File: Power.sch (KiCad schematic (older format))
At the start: 0 parts

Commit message: Wire up Power Schematic
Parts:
- added C? (x2): C, ~, symbol C
- added F? (x4): FUSE, ~, symbol FUSE
- added L? (x2): INDUCTOR, ~, symbol INDUCTOR
- added P?: CONN_12X2, symbol CONN_12X2
- added R?: R, ~, symbol R
- added SW?: SWITCH_INV, ~, symbol SWITCH_INV
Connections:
- net labels added: +12P, +12V, +3.3V, +5V, -12P, -12V, GND
- wire segments 0 -> 37

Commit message: Upgrade Current/Fan Output Schem Use PWM
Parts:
- removed F? (x4): FUSE, ~, symbol FUSE
- added TH? (x4): THERMISTOR, ~, symbol THERMISTOR
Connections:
- net labels added: +12C
- wire segments 37 -> 44
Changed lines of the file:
@@
 $Descr A4 11693 8268
 encoding utf-8
-Sheet 4 9
+Sheet 3 9
 Title ""
-Date "5 feb 2014"
+Date "9 feb 2014"
 Rev ""
 Comp ""
@@
 $EndComp
 $Comp
-L FUSE F?
-U 1 1 52F247FD
-P 3100 1600
-F 0 "F?" H 3200 1650 40  0000 C CNN
-F 1 "FUSE" H 3000 1550 40  0000 C CNN
-F 2 "~" H 3100 1600 60  0000 C CNN
-F 3 "~" H 3100 1600 60  0000 C CNN
-	1    3100 1600
-	1    0    0    -1
-$EndComp
-$Comp
-L FUSE F?
-U 1 1 52F24814
-P 3700 1800
-F 0 "F?" H 3800 1850 40  0000 C CNN
-F 1 "FUSE" H 3600 1750 40  0000 C CNN
-F 2 "~" H 3700 1800 60  0000 C CNN
-F 3 "~" H 3700 1800 60  0000 C CNN
-	1    3700 1800
-	1    0    0    -1
-$EndComp
-$Comp
-L FUSE F?
-U 1 1 52F2481A
-P 4350 2000
-F 0 "F?" H 4450 2050 40  0000 C CNN
-F 1 "FUSE" H 4250 1950 40  0000 C CNN
-F 2 "~" H 4350 2000 60  0000 C CNN
-F 3 "~" H 4350 2000 60  0000 C CNN
-	1    4350 2000
-	1    0    0    -1
-$EndComp
-$Comp
-L FUSE F?
-U 1 1 52F24820
-P 4750 2200
-F 0 "F?" H 4850 2250 40  0000 C CNN
-F 1 "FUSE" H 4650 2150 40  0000 C CNN
-F 2 "~" H 4750 2200 60  0000 C CNN
-F 3 "~" H 4750 2200 60  0000 C CNN
-	1    4750 2200
-	1    0    0    -1
-$EndComp
-$Comp
 L SWITCH_INV SW?
 U 1 1 52F24828
@@
 $EndComp
 Wire Wire Line
-	900  1700 1850 1700
+	900  1700 1500 1700
+Wire Wire Line
+	1500 1700 1850 1700
 Wire Wire Line
 	900  1700 900  1850
 Wire Wire Line
-	2650 1600 2850 1600
-Wire Wire Line
-	3300 1600 3800 1600
+	3400 1600 3800 1600
 Wire Wire Line
 	3800 1600 3800 1000
@@
 	2850 1700 2850 1800
 Wire Wire Line
-	2650 1800 3450 1800
+	2650 1800 2850 1800
+Wire Wire Line
+	2850 1800 3450 1800
 Connection ~ 2850 1800
 Wire Wire Line
@@
 	4200 1800 4200 1000
 Wire Wire Line
-	2650 2000 4100 2000
+	2650 2000 2750 2000
+Wire Wire Line
+	2750 2000 4100 2000
 Wire Wire Line
 	2650 2200 4500 2200
@@
 $EndComp
 Wire Wire Line
-	7800 2400 9000 2400
-Wire Wire Line
-	8450 1750 8450 2000
-Wire Wire Line
-	7800 1350 9050 1350
+	7800 2400 8450 2400
+Wire Wire Line
+	8450 2400 9000 2400
+Wire Wire Line
+	8450 1750 8450 1850
+Wire Wire Line
+	8450 1850 8450 2000
+Wire Wire Line
+	7800 1350 8450 1350
+Wire Wire Line
+	8450 1350 9050 1350
 Wire Wire Line
 	8000 1900 8000 1850
@@
 Wire Wire Line
 	6950 1350 7200 1350
+$Comp
+L THERMISTOR TH?
+U 1 1 52F79925
+P 3150 1600
+F 0 "TH?" V 3250 1650 50  0000 C CNN
+F 1 "THERMISTOR" V 3050 1600 50  0000 C CNN
+F 2 "~" H 3150 1600 60  0000 C CNN
+F 3 "~" H 3150 1600 60  0000 C CNN
+	1    3150 1600
+	0    -1   -1   0
+$EndComp
+$Comp
+L THERMISTOR TH?
+U 1 1 52F79932
+P 3700 1800
+F 0 "TH?" V 3800 1850 50  0000 C CNN
+F 1 "THERMISTOR" V 3600 1800 50  0000 C CNN
+F 2 "~" H 3700 1800 60  0000 C CNN
+F 3 "~" H 3700 1800 60  0000 C CNN
+	1    3700 1800
+	0    -1   -1   0
+$EndComp
+$Comp
+L THERMISTOR TH?
+U 1 1 52F79938
+P 4350 2000
+F 0 "TH?" V 4450 2050 50  0000 C CNN
+F 1 "THERMISTOR" V 4250 2000 50  0000 C CNN
+F 2 "~" H 4350 2000 60  0000 C CNN
+F 3 "~" H 4350 2000 60  0000 C CNN
+	1    4350 2000
+	0    -1   -1   0
+$EndComp
+$Comp
+L THERMISTOR TH?
+U 1 1 52F7993E
+P 4750 2200
+F 0 "TH?" V 4850 2250 50  0000 C CNN
+F 1 "THERMISTOR" V 4650 2200 50  0000 C CNN
+F 2 "~" H 4750 2200 60  0000 C CNN
+F 3 "~" H 4750 2200 60  0000 C CNN
+	1    4750 2200
+	0    -1   -1   0
+$EndComp
+Wire Wire Line
+	2900 1600 2650 1600
+Wire Wire Line
+	2750 2000 2750 1200
+Connection ~ 2750 2000
+$Comp
+L +12C #PWR?
+U 1 1 52F7999C
+P 2750 1200
+F 0 "#PWR?" H 2750 1170 30  0001 C CNN
+F 1 "+12C" H 2750 1310 40  0000 C CNN
+F 2 "" H 2750 1200 60  0000 C CNN
+F 3 "" H 2750 1200 60  0000 C CNN
+	1    2750 1200
+	1    0    0    -1
+$EndComp
 $EndSCHEMATC

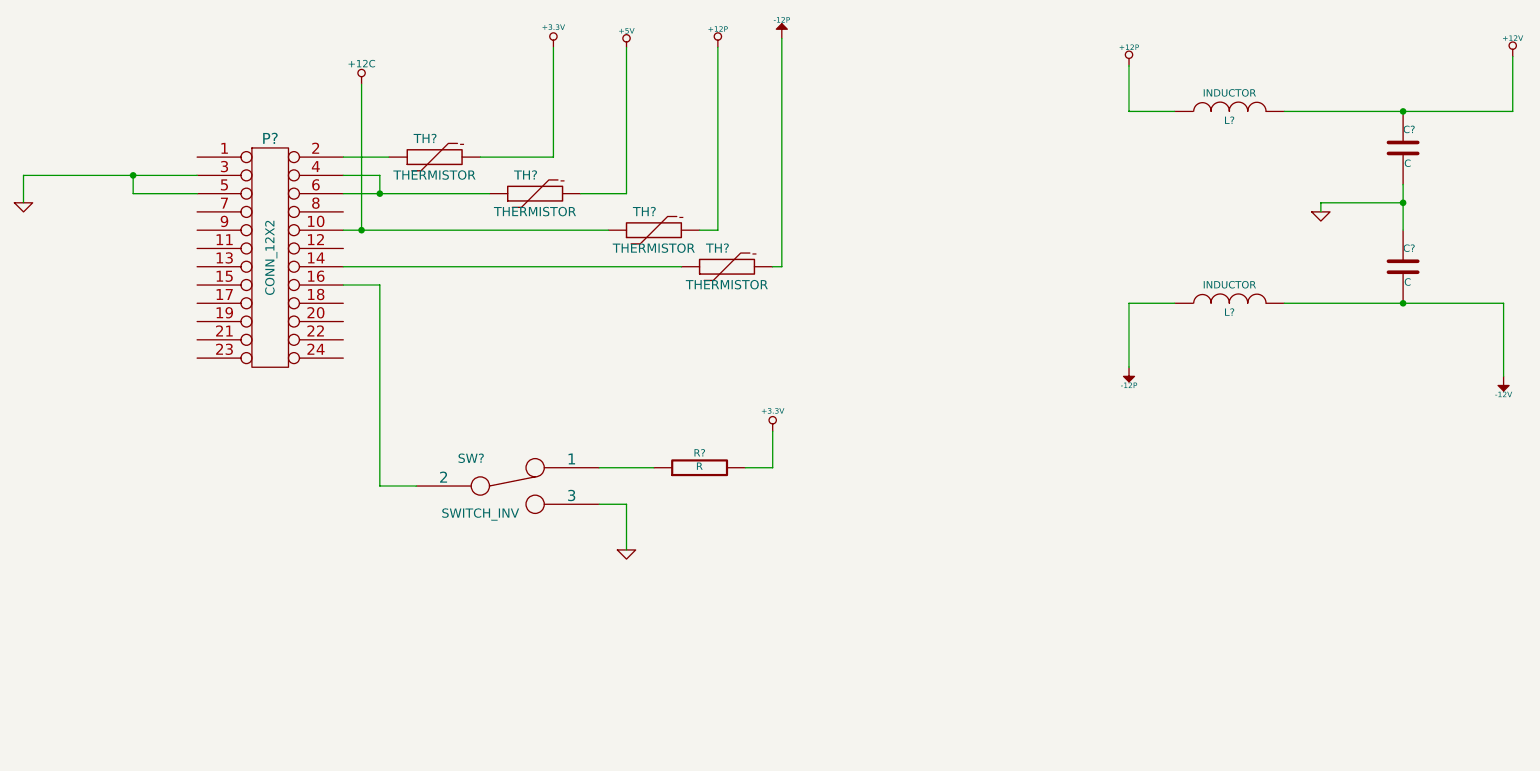
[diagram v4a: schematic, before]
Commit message: Added Arduino Connect Pin Layout
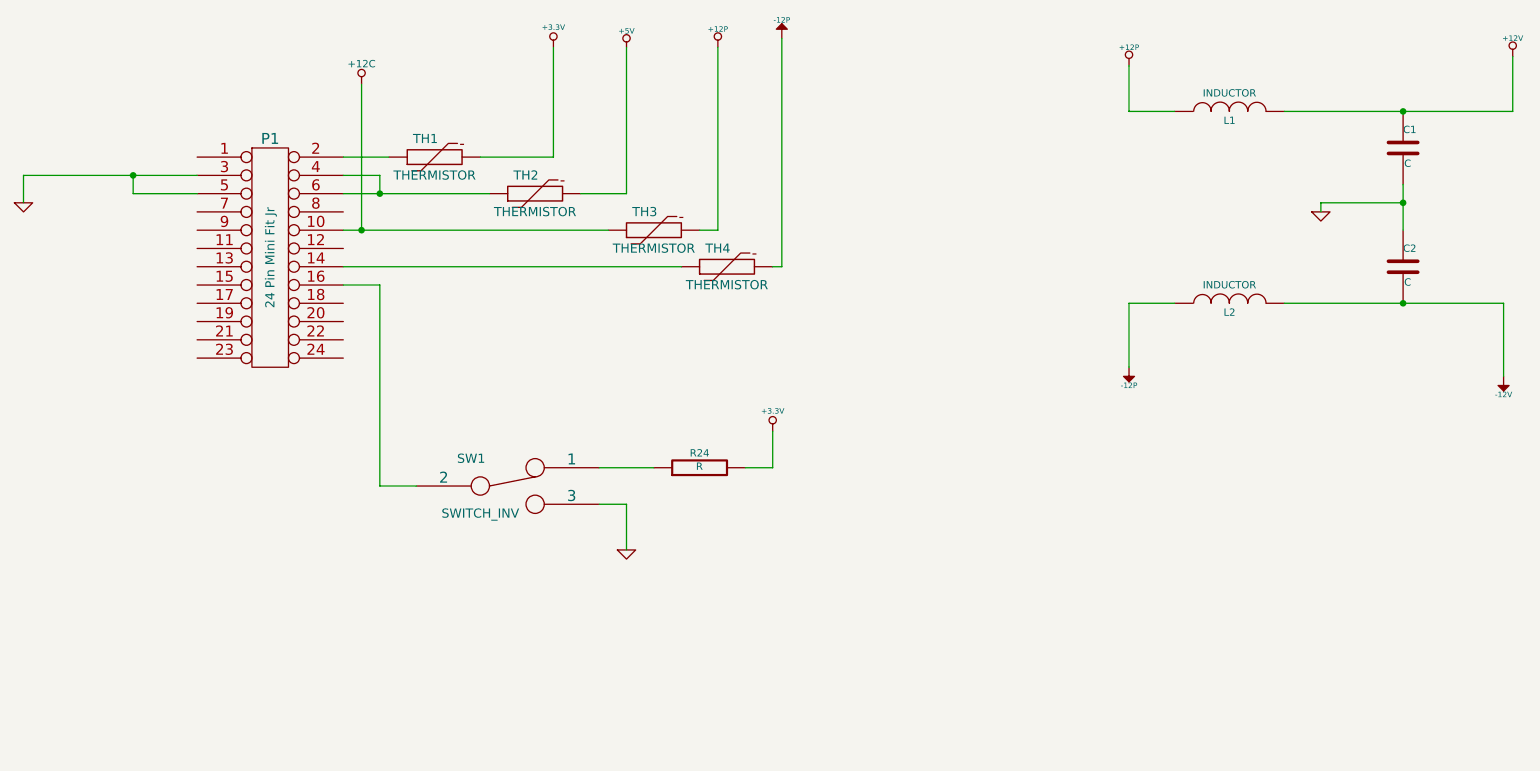
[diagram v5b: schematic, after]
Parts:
- P1: renamed from P?; value CONN_12X2 -> 24 Pin Mini Fit Jr; MFG Name (none) -> Molex; MFG Part Number (none) -> 39-30-1240
- gave numbers to parts that had none: 10
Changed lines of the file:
@@
 $EndDescr
 $Comp
-L CONN_12X2 P?
+L CONN_12X2 P1
 U 1 1 52F24792
 P 2250 2150
-F 0 "P?" H 2250 2800 60  0000 C CNN
-F 1 "CONN_12X2" V 2250 2150 50  0000 C CNN
+F 0 "P1" H 2250 2800 60  0000 C CNN
+F 1 "24 Pin Mini Fit Jr" V 2250 2150 50  0000 C CNN
 F 2 "" H 2250 2150 60  0000 C CNN
 F 3 "" H 2250 2150 60  0000 C CNN
+F 4 "Molex" H 2250 2150 60  0001 C CNN "MFG Name"
+F 5 "39-30-1240" H 2250 2150 60  0001 C CNN "MFG Part Number"
 	1    2250 2150
 	1    0    0    -1
 $EndComp
 $Comp
-L GND #PWR?
+L GND #PWR3
 U 1 1 52F247A1
 P 900 1850
-F 0 "#PWR?" H 900 1850 30  0001 C CNN
+F 0 "#PWR3" H 900 1850 30  0001 C CNN
 F 1 "GND" H 900 1780 30  0001 C CNN
 F 2 "" H 900 1850 60  0000 C CNN
@@
 $EndComp
 $Comp
-L +3.3V #PWR?
+L +3.3V #PWR5
 U 1 1 52F247B1
 P 3800 1000
-F 0 "#PWR?" H 3800 960 30  0001 C CNN
+F 0 "#PWR5" H 3800 960 30  0001 C CNN
 F 1 "+3.3V" H 3800 1110 30  0000 C CNN
 F 2 "" H 3800 1000 60  0000 C CNN
@@
 $EndComp
 $Comp
-L +5V #PWR?
+L +5V #PWR6
 U 1 1 52F247C3
 P 4200 1000
-F 0 "#PWR?" H 4200 1090 20  0001 C CNN
+F 0 "#PWR6" H 4200 1090 20  0001 C CNN
 F 1 "+5V" H 4200 1090 30  0000 C CNN
 F 2 "" H 4200 1000 60  0000 C CNN
@@
 $EndComp
 $Comp
-L SWITCH_INV SW?
+L SWITCH_INV SW1
 U 1 1 52F24828
 P 3550 3400
-F 0 "SW?" H 3350 3550 50  0000 C CNN
+F 0 "SW1" H 3350 3550 50  0000 C CNN
 F 1 "SWITCH_INV" H 3400 3250 50  0000 C CNN
 F 2 "~" H 3550 3400 60  0000 C CNN
@@
 $EndComp
 $Comp
-L +12P #PWR?
+L +12P #PWR8
 U 1 1 52F248B4
 P 4700 1000
-F 0 "#PWR?" H 4700 970 30  0001 C CNN
+F 0 "#PWR8" H 4700 970 30  0001 C CNN
 F 1 "+12P" H 4700 1100 30  0000 C CNN
 F 2 "" H 4700 1000 60  0000 C CNN
@@
 $EndComp
 $Comp
-L -12P #PWR?
+L -12P #PWR10
 U 1 1 52F24F25
 P 5050 950
-F 0 "#PWR?" H 5050 1080 20  0001 C CNN
+F 0 "#PWR10" H 5050 1080 20  0001 C CNN
 F 1 "-12P" H 5050 1050 30  0000 C CNN
 F 2 "" H 5050 950 60  0000 C CNN
@@
 $EndComp
 $Comp
-L GND #PWR?
+L GND #PWR7
 U 1 1 52F24F77
 P 4200 3750
-F 0 "#PWR?" H 4200 3750 30  0001 C CNN
+F 0 "#PWR7" H 4200 3750 30  0001 C CNN
 F 1 "GND" H 4200 3680 30  0001 C CNN
 F 2 "" H 4200 3750 60  0000 C CNN
@@
 $EndComp
 $Comp
-L R R?
+L R R24
 U 1 1 52F24FB1
 P 4600 3300
-F 0 "R?" V 4680 3300 40  0000 C CNN
+F 0 "R24" V 4680 3300 40  0000 C CNN
 F 1 "R" V 4607 3301 40  0000 C CNN
 F 2 "~" V 4530 3300 30  0000 C CNN
@@
 $EndComp
 $Comp
-L +3.3V #PWR?
+L +3.3V #PWR9
 U 1 1 52F24FD9
 P 5000 3100
-F 0 "#PWR?" H 5000 3060 30  0001 C CNN
+F 0 "#PWR9" H 5000 3060 30  0001 C CNN
 F 1 "+3.3V" H 5000 3210 30  0000 C CNN
 F 2 "" H 5000 3100 60  0000 C CNN
@@
 $EndComp
 Wire Wire Line
-	900  1700 1500 1700
-Wire Wire Line
-	1500 1700 1850 1700
+	900  1700 1850 1700
 Wire Wire Line
 	900  1700 900  1850
@@
 	2850 1700 2850 1800
 Wire Wire Line
-	2650 1800 2850 1800
-Wire Wire Line
-	2850 1800 3450 1800
+	2650 1800 3450 1800
 Connection ~ 2850 1800
 Wire Wire Line
@@
 	4200 1800 4200 1000
 Wire Wire Line
-	2650 2000 2750 2000
-Wire Wire Line
-	2750 2000 4100 2000
+	2650 2000 4100 2000
 Wire Wire Line
 	2650 2200 4500 2200
@@
 	5000 3100 5000 3300
 $Comp
-L -12P #PWR?
+L -12P #PWR12
 U 1 1 52F251E3
 P 6950 2750
-F 0 "#PWR?" H 6950 2880 20  0001 C CNN
+F 0 "#PWR12" H 6950 2880 20  0001 C CNN
 F 1 "-12P" H 6950 2850 30  0000 C CNN
 F 2 "" H 6950 2750 60  0000 C CNN
@@
 $EndComp
 $Comp
-L +12P #PWR?
+L +12P #PWR11
 U 1 1 52F251E9
 P 6950 1100
-F 0 "#PWR?" H 6950 1070 30  0001 C CNN
+F 0 "#PWR11" H 6950 1070 30  0001 C CNN
 F 1 "+12P" H 6950 1200 30  0000 C CNN
 F 2 "" H 6950 1100 60  0000 C CNN
@@
 $EndComp
 $Comp
-L GND #PWR?
+L GND #PWR13
 U 1 1 52F251EF
 P 8000 1900
-F 0 "#PWR?" H 8000 1900 30  0001 C CNN
+F 0 "#PWR13" H 8000 1900 30  0001 C CNN
 F 1 "GND" H 8000 1830 30  0001 C CNN
 F 2 "" H 8000 1900 60  0000 C CNN
@@
 $EndComp
 $Comp
-L INDUCTOR L?
+L INDUCTOR L1
 U 1 1 52F2522D
 P 7500 1350
-F 0 "L?" V 7450 1350 40  0000 C CNN
+F 0 "L1" V 7450 1350 40  0000 C CNN
 F 1 "INDUCTOR" V 7600 1350 40  0000 C CNN
 F 2 "~" H 7500 1350 60  0000 C CNN
@@
 $EndComp
 $Comp
-L INDUCTOR L?
+L INDUCTOR L2
 U 1 1 52F2523A
 P 7500 2400
-F 0 "L?" V 7450 2400 40  0000 C CNN
+F 0 "L2" V 7450 2400 40  0000 C CNN
 F 1 "INDUCTOR" V 7600 2400 40  0000 C CNN
 F 2 "~" H 7500 2400 60  0000 C CNN
@@
 $EndComp
 $Comp
-L C C?
+L C C1
 U 1 1 52F25242
 P 8450 1550
-F 0 "C?" H 8450 1650 40  0000 L CNN
+F 0 "C1" H 8450 1650 40  0000 L CNN
 F 1 "C" H 8456 1465 40  0000 L CNN
 F 2 "~" H 8488 1400 30  0000 C CNN
@@
 $EndComp
 $Comp
-L C C?
+L C C2
 U 1 1 52F2524F
 P 8450 2200
-F 0 "C?" H 8450 2300 40  0000 L CNN
+F 0 "C2" H 8450 2300 40  0000 L CNN
 F 1 "C" H 8456 2115 40  0000 L CNN
 F 2 "~" H 8488 2050 30  0000 C CNN
@@
 $EndComp
 Wire Wire Line
-	7800 2400 8450 2400
-Wire Wire Line
-	8450 2400 9000 2400
-Wire Wire Line
-	8450 1750 8450 1850
-Wire Wire Line
-	8450 1850 8450 2000
-Wire Wire Line
-	7800 1350 8450 1350
-Wire Wire Line
-	8450 1350 9050 1350
+	7800 2400 9000 2400
+Wire Wire Line
+	8450 1750 8450 2000
+Wire Wire Line
+	7800 1350 9050 1350
 Wire Wire Line
 	8000 1900 8000 1850
@@
 Connection ~ 8450 1850
 $Comp
-L +12V #PWR?
+L +12V #PWR15
 U 1 1 52F2533A
 P 9050 1050
-F 0 "#PWR?" H 9050 1000 20  0001 C CNN
+F 0 "#PWR15" H 9050 1000 20  0001 C CNN
 F 1 "+12V" H 9050 1150 30  0000 C CNN
 F 2 "" H 9050 1050 60  0000 C CNN
@@
 $EndComp
 $Comp
-L -12V #PWR?
+L -12V #PWR14
 U 1 1 52F25349
 P 9000 2800
-F 0 "#PWR?" H 9000 2930 20  0001 C CNN
+F 0 "#PWR14" H 9000 2930 20  0001 C CNN
 F 1 "-12V" H 9000 2900 30  0000 C CNN
 F 2 "" H 9000 2800 60  0000 C CNN
@@
 	6950 1350 7200 1350
 $Comp
-L THERMISTOR TH?
+L THERMISTOR TH1
 U 1 1 52F79925
 P 3150 1600
-F 0 "TH?" V 3250 1650 50  0000 C CNN
+F 0 "TH1" V 3250 1650 50  0000 C CNN
 F 1 "THERMISTOR" V 3050 1600 50  0000 C CNN
 F 2 "~" H 3150 1600 60  0000 C CNN
@@
 $EndComp
 $Comp
-L THERMISTOR TH?
+L THERMISTOR TH2
 U 1 1 52F79932
 P 3700 1800
-F 0 "TH?" V 3800 1850 50  0000 C CNN
+F 0 "TH2" V 3800 1850 50  0000 C CNN
 F 1 "THERMISTOR" V 3600 1800 50  0000 C CNN
 F 2 "~" H 3700 1800 60  0000 C CNN
@@
 $EndComp
 $Comp
-L THERMISTOR TH?
+L THERMISTOR TH3
 U 1 1 52F79938
 P 4350 2000
-F 0 "TH?" V 4450 2050 50  0000 C CNN
+F 0 "TH3" V 4450 2050 50  0000 C CNN
 F 1 "THERMISTOR" V 4250 2000 50  0000 C CNN
 F 2 "~" H 4350 2000 60  0000 C CNN
@@
 $EndComp
 $Comp
-L THERMISTOR TH?
+L THERMISTOR TH4
 U 1 1 52F7993E
 P 4750 2200
-F 0 "TH?" V 4850 2250 50  0000 C CNN
+F 0 "TH4" V 4850 2250 50  0000 C CNN
 F 1 "THERMISTOR" V 4650 2200 50  0000 C CNN
 F 2 "~" H 4750 2200 60  0000 C CNN
@@
 Connection ~ 2750 2000
 $Comp
-L +12C #PWR?
+L +12C #PWR4
 U 1 1 52F7999C
 P 2750 1200
-F 0 "#PWR?" H 2750 1170 30  0001 C CNN
+F 0 "#PWR4" H 2750 1170 30  0001 C CNN
 F 1 "+12C" H 2750 1310 40  0000 C CNN
 F 2 "" H 2750 1200 60  0000 C CNN

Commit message: Associate and Place Power Component
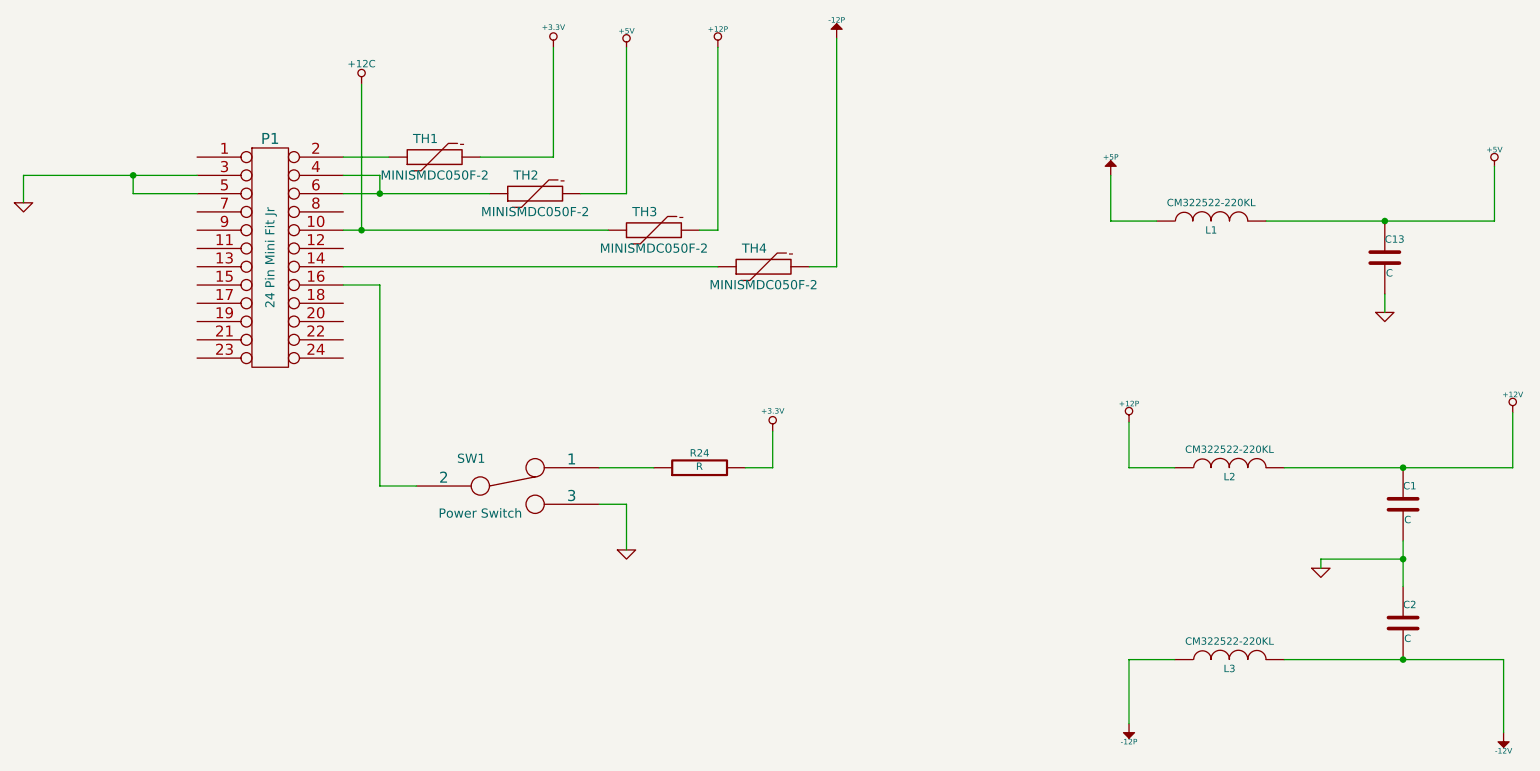
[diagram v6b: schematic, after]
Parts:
- removed L2: INDUCTOR, ~, symbol INDUCTOR
- added C13: C, ~, symbol C
- added L1, L3: CM322522-220KL, ~, symbol INDUCTOR
- L2: renamed from L1; value INDUCTOR -> CM322522-220KL; MFG Name (none) -> Bournes; MFG Part Number (none) -> CM322522-220KL
- SW1: value SWITCH_INV -> Power Switch; MFG Name (none) -> C&K Components; MFG Part Number (none) -> OS102011MA1QN1
- TH1, TH2, TH3, TH4: value THERMISTOR -> MINISMDC050F-2; MFG Name (none) -> TE Connectivity; MFG Part Number (none) -> MINISMDC050F-2
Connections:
- net +5V: now also C13.1, L1.2
- net -12P: now also L3.1
- net -12V: now also L3.2
- net GND: now also C13.2
- new net +5P: L1.1
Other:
- moved on the sheet: C1, C2, L2
